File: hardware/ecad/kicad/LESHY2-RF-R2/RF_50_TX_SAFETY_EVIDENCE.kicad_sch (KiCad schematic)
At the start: 98 parts, among them J13 Samtec FTSH-105-01-L-DV-K-P-TR, Q6 Diodes Incorporated 2N7002DW-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, SW5 C&K JS102011SCQN, U101 Diodes Incorporated BAT54-7-F, U102 TLV1821DCKR, U103 TLV1821DCKR, U104 TLV1821DCKR, U105 TCA9535PWR, U106 BAT54ALT1G, U107 BAT54ALT1G, U108 BAT54ALT1G, U109 BAT54ALT1G, U110 BAT54ALT1G, U111 74LVC2G14GV,125, U112 SN74LVC3G07DCUR, U113 SN74LVC08APWR, U114 SN74LVC1G74DCUR, U115 74LVC1G32GV,125, U116 SN74LVC1G17DCKR, U117 Texas Instruments SN74LVC1G06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, U118 SN74LVC1G07DCKR, U119 TPS3808G33DBVR, U120 Texas Instruments TPD4E05U06D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, U121 Texas Instruments MSPM0C1106S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, U122 SN74LVC1G07DCKR, U123 SN74LVC1G07DCKR, U124 Texas Instruments TPS3435CAKA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, U125 SN74LVC1G07DCKR, U126 SN74LVC1G07DCKR, U127 Diodes Incorporated BAT54-7-F, U128 Diodes Incorporated BAT54-7-F

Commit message: Connect RF emergency reset to active RP reset net
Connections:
- net RP_RESET_N renamed RF_RP_RESET_N
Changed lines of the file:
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@@
 		(effects (font (size 1.27 1.27)))
 	)
-	(label "RP_RESET_N"
+	(hierarchical_label "RF_RP_RESET_N"
+		(shape bidirectional)
 		(at 401.32 125.73 0)
 		(effects (font (size 1.27 1.27)))
@@
 		(effects (font (size 1.27 1.27)) (justify right bottom))
 	)
-	(label "RP_RESET_N"
+	(label "RF_RP_RESET_N"
 		(at 990.60 266.70 180)
 		(effects (font (size 1.27 1.27)) (justify right bottom))

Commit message: Review R2 startup and fault-display sequencing
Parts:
- removed R251: Yageo RC0402FR-0710KL, Resistor_SMD:R_0402_1005Metric, symbol Leshy2_R2:yageo_rc0402fr_0710kl
- added R265: Yageo RC0402FR-0710KL, Resistor_SMD:R_0402_1005Metric, symbol Leshy2_R2:yageo_rc0402fr_0710kl
- renumbered R252 to R251, R253 to R252, R254 to R253, R255 to R254, R256 to R255, R257 to R256, R258 to R257, R259 to R258, R260 to R259, R261 to R260, R262 to R261, R263 to R262, R264 to R263, R265 to R264
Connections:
- net EVIDENCE_MASK_UNUSED_P17 is gone; now on net SAFETY_GROUND: U105.20 (P17)
- net FAULT_ASSERT_N: no longer U123.4 (Y)
- net S3_FAULT_RESET_REQUEST: now also R265.1 (END_1)
- net SAFETY_GROUND: now also R265.2 (END_2)
- new net S3_RESET_KILL_GATE: U123.4 (Y)
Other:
- moved on the sheet: R251, R252, R253, R254, R255, R256, R257, R258, R259, R260, R261, R262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

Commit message: Review R2 power transitions and watchdog
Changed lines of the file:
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@@
 		(effects (font (size 1.27 1.27)))
 	)
-	(label "FAULT_KILL"
+	(hierarchical_label "FAULT_KILL"
+		(shape bidirectional)
 		(at 309.88 269.24 0)
 		(effects (font (size 1.27 1.27)))

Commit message: Verify factory-placeable Airband filter
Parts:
- renumbered C254 to C253, C255 to C254, C256 to C255, C257 to C256, C258 to C257, C259 to C258, C260 to C259, C261 to C260, C262 to C261, C263 to C262, C264 to C263, C265 to C264, C266 to C265, C267 to C266, C268 to C267, C269 to C268, C270 to C269, C271 to C270, C272 to C271, C273 to C272, C274 to C273, C275 to C274, C276 to C275, C277 to C276, C278 to C277, C279 to C278, C280 to C279
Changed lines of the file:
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@@
 		(on_board yes)
 		(dnp no)
-		(property "Reference" "C254"
+		(property "Reference" "C253"
 			(at 55.88 44.45 0)
 			(show_name no)
@@
 			(project "LESHY2-RF-R2"
 				(path "/6d47ec69-d4e6-5f0a-87ca-f1fb82f96328"
-					(reference "C254")
+					(reference "C253")
 					(unit 1)
 				)
@@
 		(on_board yes)
 		(dnp no)
-		(property "Reference" "C255"
+		(property "Reference" "C254"
 			(at 147.32 44.45 0)
 			(show_name no)
@@
 			(project "LESHY2-RF-R2"
 				(path "/6d47ec69-d4e6-5f0a-87ca-f1fb82f96328"
-					(reference "C255")
+					(reference "C254")
 					(unit 1)
 				)
@@
 		(on_board yes)
 		(dnp no)
-		(property "Reference" "C256"
+		(property "Reference" "C255"
 			(at 238.76 44.45 0)
 			(show_name no)
@@
 			(project "LESHY2-RF-R2"
 				(path "/6d47ec69-d4e6-5f0a-87ca-f1fb82f96328"
-					(reference "C256")
+					(reference "C255")
 					(unit 1)
 				)
@@
 		(on_board yes)
 		(dnp no)
-		(property "Reference" "C257"
+		(property "Reference" "C256"
 			(at 330.20 44.45 0)
 			(show_name no)
@@
 			(project "LESHY2-RF-R2"
 				(path "/6d47ec69-d4e6-5f0a-87ca-f1fb82f96328"
-					(reference "C257")
+					(reference "C256")
 					(unit 1)
 				)
@@
 		(on_board yes)
 		(dnp no)
-		(property "Reference" "C258"
+		(property "Reference" "C257"
 			(at 421.64 44.45 0)
 			(show_name no)
@@
 			(project "LESHY2-RF-R2"
 				(path "/6d47ec69-d4e6-5f0a-87ca-f1fb82f96328"
-					(reference "C258")
+					(reference "C257")
 					(unit 1)
 				)
@@
 		(on_board yes)
 		(dnp no)
-		(property "Reference" "C259"
+		(property "Reference" "C258"
 			(at 513.08 44.45 0)
 			(show_name no)
@@
 			(project "LESHY2-RF-R2"
 				(path "/6d47ec69-d4e6-5f0a-87ca-f1fb82f96328"
-					(reference "C259")
+					(reference "C258")
 					(unit 1)
 				)
@@
 		(on_board yes)
 		(dnp no)
-		(property "Reference" "C260"
+		(property "Reference" "C259"
 			(at 604.52 44.45 0)
 			(show_name no)
@@
 			(project "LESHY2-RF-R2"
 				(path "/6d47ec69-d4e6-5f0a-87ca-f1fb82f96328"
-					(reference "C260")
+					(reference "C259")
 					(unit 1)
 				)
@@
 		(on_board yes)
 		(dnp no)
-		(property "Reference" "C261"
+		(property "Reference" "C260"
 			(at 695.96 44.45 0)
 			(show_name no)
@@
 			(project "LESHY2-RF-R2"
 				(path "/6d47ec69-d4e6-5f0a-87ca-f1fb82f96328"
-					(reference "C261")
+					(reference "C260")
 					(unit 1)
 				)
@@
 		(on_board yes)
 		(dnp no)
-		(property "Reference" "C262"
+		(property "Reference" "C261"
 			(at 787.40 44.45 0)
 			(show_name no)
@@
 			(project "LESHY2-RF-R2"
 				(path "/6d47ec69-d4e6-5f0a-87ca-f1fb82f96328"
-					(reference "C262")
+					(reference "C261")
 					(unit 1)
 				)
@@
 		(on_board yes)
 		(dnp no)
-		(property "Reference" "C263"
+		(property "Reference" "C262"
 			(at 878.84 44.45 0)
 			(show_name no)
@@
 			(project "LESHY2-RF-R2"
 				(path "/6d47ec69-d4e6-5f0a-87ca-f1fb82f96328"
-					(reference "C263")
+					(reference "C262")
 					(unit 1)
 				)
@@
 		(on_board yes)
 		(dnp no)
-		(property "Reference" "C264"
+		(property "Reference" "C263"
 			(at 970.28 44.45 0)
 			(show_name no)
@@
 			(project "LESHY2-RF-R2"
 				(path "/6d47ec69-d4e6-5f0a-87ca-f1fb82f96328"
-					(reference "C264")
+					(reference "C263")
 					(unit 1)
 				)
@@
 		(on_board yes)
 		(dnp no)
-		(property "Reference" "C265"
+		(property "Reference" "C264"
 			(at 1061.72 44.45 0)
 			(show_name no)
@@
 			(project "LESHY2-RF-R2"
 				(path "/6d47ec69-d4e6-5f0a-87ca-f1fb82f96328"
-					(reference "C265")
+					(reference "C264")
 					(unit 1)
 				)
@@
 		(on_board yes)
 		(dnp no)
-		(property "Reference" "C266"
+		(property "Reference" "C265"
 			(at 55.88 80.01 0)
 			(show_name no)
@@
 			(project "LESHY2-RF-R2"
 				(path "/6d47ec69-d4e6-5f0a-87ca-f1fb82f96328"
-					(reference "C266")
+					(reference "C265")
 					(unit 1)
 				)
@@
 		(on_board yes)
 		(dnp no)
-		(property "Reference" "C267"
+		(property "Reference" "C266"
 			(at 147.32 80.01 0)
 			(show_name no)
@@
 			(project "LESHY2-RF-R2"
 				(path "/6d47ec69-d4e6-5f0a-87ca-f1fb82f96328"
-					(reference "C267")
+					(reference "C266")
 					(unit 1)
 				)
@@
 		(on_board yes)
 		(dnp no)
-		(property "Reference" "C268"
+		(property "Reference" "C267"
 			(at 238.76 80.01 0)
 			(show_name no)
@@
 			(project "LESHY2-RF-R2"
 				(path "/6d47ec69-d4e6-5f0a-87ca-f1fb82f96328"
-					(reference "C268")
+					(reference "C267")
 					(unit 1)
 				)
@@
 		(on_board yes)
 		(dnp no)
-		(property "Reference" "C269"
+		(property "Reference" "C268"
 			(at 330.20 80.01 0)
 			(show_name no)
@@
 			(project "LESHY2-RF-R2"
 				(path "/6d47ec69-d4e6-5f0a-87ca-f1fb82f96328"
-					(reference "C269")
+					(reference "C268")
 					(unit 1)
 				)
@@
 		(on_board yes)
 		(dnp no)
-		(property "Reference" "C270"
+		(property "Reference" "C269"
 			(at 421.64 80.01 0)
 			(show_name no)
@@
 			(project "LESHY2-RF-R2"
 				(path "/6d47ec69-d4e6-5f0a-87ca-f1fb82f96328"
-					(reference "C270")
+					(reference "C269")
 					(unit 1)
 				)
@@
 		(on_board yes)
 		(dnp no)
-		(property "Reference" "C271"
+		(property "Reference" "C270"
 			(at 513.08 80.01 0)
 			(show_name no)
@@
 			(project "LESHY2-RF-R2"
 				(path "/6d47ec69-d4e6-5f0a-87ca-f1fb82f96328"
-					(reference "C271")
+					(reference "C270")
 					(unit 1)
 				)
@@
 		(on_board yes)
 		(dnp no)
-		(property "Reference" "C272"
+		(property "Reference" "C271"
 			(at 604.52 80.01 0)
 			(show_name no)
@@
 			(project "LESHY2-RF-R2"
 				(path "/6d47ec69-d4e6-5f0a-87ca-f1fb82f96328"
-					(reference "C272")
+					(reference "C271")
 					(unit 1)
 				)
@@
 		(on_board yes)
 		(dnp no)
-		(property "Reference" "C273"
+		(property "Reference" "C272"
 			(at 695.96 80.01 0)
 			(show_name no)
@@
 			(project "LESHY2-RF-R2"
 				(path "/6d47ec69-d4e6-5f0a-87ca-f1fb82f96328"
-					(reference "C273")
+					(reference "C272")
 					(unit 1)
 				)
@@
 		(on_board yes)
 		(dnp no)
-		(property "Reference" "C274"
+		(property "Reference" "C273"
 			(at 787.40 80.01 0)
 			(show_name no)
@@
 			(project "LESHY2-RF-R2"
 				(path "/6d47ec69-d4e6-5f0a-87ca-f1fb82f96328"
-					(reference "C274")
+					(reference "C273")
 					(unit 1)
 				)
@@
 		(on_board yes)
 		(dnp no)
-		(property "Reference" "C275"
+		(property "Reference" "C274"
 			(at 878.84 80.01 0)
 			(show_name no)
@@
 			(project "LESHY2-RF-R2"
 				(path "/6d47ec69-d4e6-5f0a-87ca-f1fb82f96328"
-					(reference "C275")
+					(reference "C274")
 					(unit 1)
 				)
@@
 		(on_board yes)
 		(dnp no)
-		(property "Reference" "C276"
+		(property "Reference" "C275"
 			(at 970.28 80.01 0)
 			(show_name no)
@@
 			(project "LESHY2-RF-R2"
 				(path "/6d47ec69-d4e6-5f0a-87ca-f1fb82f96328"
-					(reference "C276")
+					(reference "C275")
 					(unit 1)
 				)
@@
 		(on_board yes)
 		(dnp no)
-		(property "Reference" "C277"
+		(property "Reference" "C276"
 			(at 1061.72 80.01 0)
 			(show_name no)
@@
 			(project "LESHY2-RF-R2"
 				(path "/6d47ec69-d4e6-5f0a-87ca-f1fb82f96328"
-					(reference "C277")
+					(reference "C276")
 					(unit 1)
 				)
@@
 		(on_board yes)
 		(dnp no)
-		(property "Reference" "C278"
+		(property "Reference" "C277"
 			(at 55.88 115.57 0)
 			(show_name no)
@@
 			(project "LESHY2-RF-R2"
 				(path "/6d47ec69-d4e6-5f0a-87ca-f1fb82f96328"
-					(reference "C278")
+					(reference "C277")
 					(unit 1)
 				)
@@
 		(on_board yes)
 		(dnp no)
-		(property "Reference" "C279"
+		(property "Reference" "C278"
 			(at 147.32 115.57 0)
 			(show_name no)
@@
 			(project "LESHY2-RF-R2"
 				(path "/6d47ec69-d4e6-5f0a-87ca-f1fb82f96328"
-					(reference "C279")
+					(reference "C278")
 					(unit 1)
 				)
@@
 		(on_board yes)
 		(dnp no)
-		(property "Reference" "C280"
+		(property "Reference" "C279"
 			(at 238.76 115.57 0)
 			(show_name no)
@@
 			(project "LESHY2-RF-R2"
 				(path "/6d47ec69-d4e6-5f0a-87ca-f1fb82f96328"
-					(reference "C280")
-					(unit 1)
-				)
+					(reference "C279")
+					(unit 1)
+				)

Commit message: Complete current R2 schematic and sourcing revalidation
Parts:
- renumbered C253 to C262, C254 to C263, C255 to C264, C256 to C265, C257 to C266, C258 to C267, C259 to C268, C260 to C269, C261 to C270, C262 to C271, C263 to C272, C264 to C273, C265 to C274, C266 to C275, C267 to C276, C268 to C277, C269 to C278, C270 to C279, C271 to C280, C272 to C281, C273 to C282, C274 to C283, C275 to C284, C276 to C285, C277 to C286, C278 to C287, C279 to C288, R240 to R249, R241 to R250, R242 to R251, R243 to R252, R244 to R253, R245 to R254, R246 to R255, R247 to R256, R248 to R257, R249 to R258, R250 to R259, R251 to R260, R252 to R261, R253 to R262, R254 to R263, R255 to R264, R256 to R265, R257 to R266, R258 to R267, R259 to R268, R260 to R269, R261 to R270, R262 to R271, R263 to R272, R264 to R273, R265 to R274, R266 to R275, R267 to R276, R268 to R277, R269 to R278, R270 to R279, R271 to R280, R272 to R281, R273 to R282, R274 to R283, R275 to R284, R276 to R285, R277 to R286, R278 to R287, R279 to R288, U101 to U107, U102 to U108, U103 to U109, U104 to U110, U105 to U111, U106 to U112, U107 to U113, U108 to U114, U109 to U115, U110 to U116, U111 to U117, U112 to U118, U113 to U119, U114 to U120, U115 to U121, U116 to U122, U117 to U123, U118 to U124, U119 to U125, U120 to U126, U121 to U127, U122 to U128, U123 to U129, U124 to U130, U125 to U131, U126 to U132, U127 to U133, U128 to U134
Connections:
- net SAFETY_GROUND: no longer U111.20 (P17)
- net EV_N9_U219_NFC: now reaches U116.2 (K2)
- net EV_N9_U219_NFC: now also U111.20 (P17)
- no-connect marks 22 -> 21

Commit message: Canonicalize physical ground anchors
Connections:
- net SAFETY_ESD_GROUND is gone; now on net POWER_GROUND: U126.3 (GND_3), U126.8 (GND_8)
- net SAFETY_GROUND is gone; now on net POWER_GROUND: C262.2 (END_2), C263.2 (END_2), C264.2 (END_2), C265.2 (END_2), C266.2 (END_2), C268.2 (END_2), C269.2 (END_2), C270.2 (END_2), C271.2 (END_2), C272.2 (END_2), C273.2 (END_2), C274.2 (END_2), C275.2 (END_2), C276.2 (END_2), C277.2 (END_2), C278.2 (END_2), C279.2 (END_2), C280.2 (END_2), C281.2 (END_2), C282.2 (END_2), C283.2 (END_2), C284.2 (END_2), C285.2 (END_2), C286.2 (END_2), C287.2 (END_2), C288.2 (END_2), J13.1 (P1), J13.7 (P7), J13.9 (P9), Q6.1 (S2), Q6.2 (G2), Q6.4 (S1), R250.2 (END_2), R253.2 (END_2), R255.2 (END_2), R256.2 (END_2), R257.2 (END_2), R258.2 (END_2), R262.2 (END_2), R273.2 (END_2), R274.2 (END_2), R276.2 (END_2), R280.2 (END_2), R283.2 (END_2), R285.2 (END_2), R287.2 (END_2), U108.2 (VMINUS), U109.2 (VMINUS), U110.2 (VMINUS), U111.12 (GND), U111.2 (A1), U111.21 (A0), U111.3 (A2), U117.2 (GND), U118.4 (GND), U119.7 (GND), U120.4 (GND), U121.3 (GND), U122.3 (GND), U123.3 (GND), U124.3 (GND), U125.2 (GND), U127.7 (VSS), U128.3 (GND), U129.3 (GND), U130.1 (SET0), U130.4 (GND), U130.5 (SET1), U131.3 (GND), U132.3 (GND)

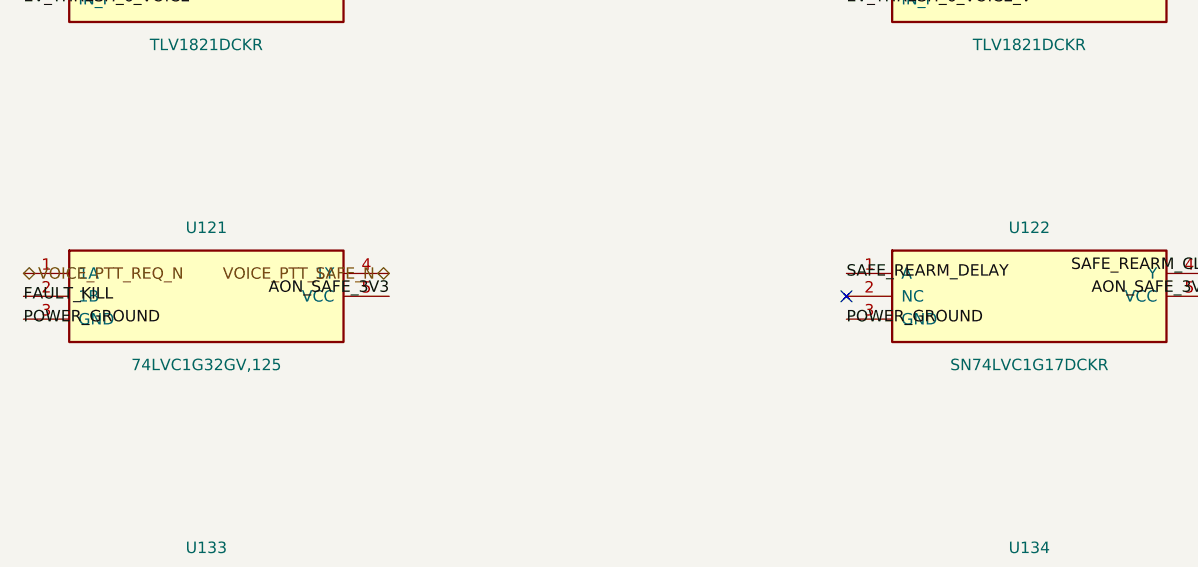
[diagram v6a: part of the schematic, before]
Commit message: Fix exact pin maps and RP flash power; add typed electrical review
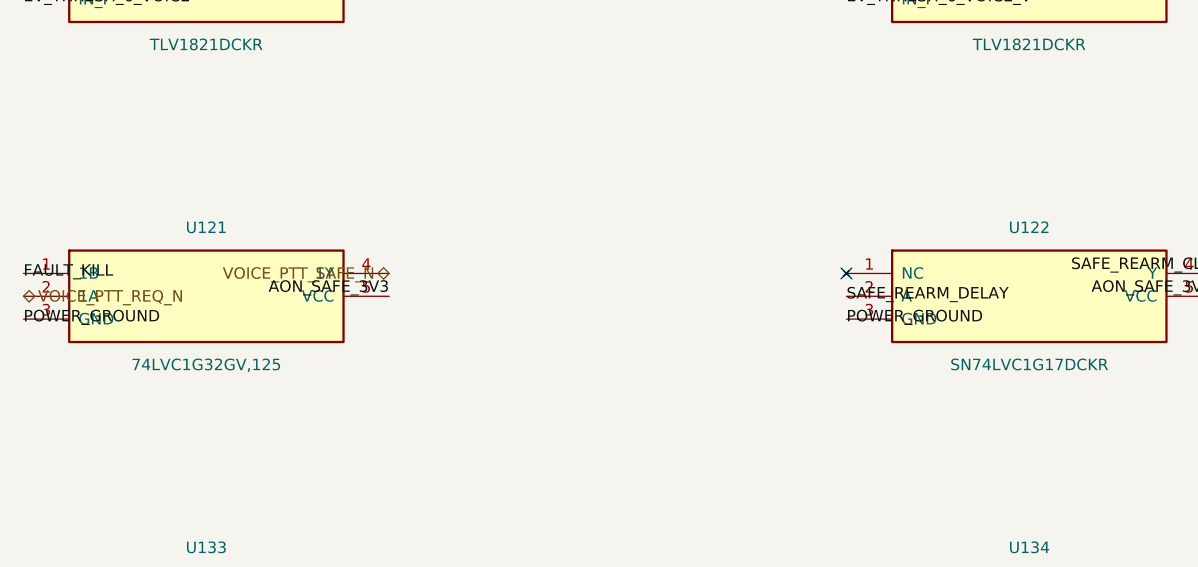
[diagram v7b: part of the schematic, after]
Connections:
- net FAULT_KILL: now also U121.1 (1B); no longer U121.2 (1B)
- net SAFE_REARM_DELAY: now also U122.2 (A); no longer U122.1 (A)
- net VOICE_PTT_REQ_N: now also U121.2 (1A); no longer U121.1 (1A)
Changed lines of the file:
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@@
 		)
+	)
+	(label "FAULT_KILL"
+		(at 35.56 298.45 0)
+		(effects (font (size 1.27 1.27)))
 	)
 	(hierarchical_label "VOICE_PTT_REQ_N"
 		(shape bidirectional)
-		(at 35.56 298.45 0)
-		(effects (font (size 1.27 1.27)))
-	)
-	(label "FAULT_KILL"
 		(at 35.56 300.99 0)
 		(effects (font (size 1.27 1.27)))
@@
 		)
 	)
+	(no_connect (at 127.00 298.45)
+	)
 	(label "SAFE_REARM_DELAY"
-		(at 127.00 298.45 0)
+		(at 127.00 300.99 0)
 		(effects (font (size 1.27 1.27)))
 	)
-	(no_connect (at 127.00 300.99)
-	)
 	(label "POWER_GROUND"

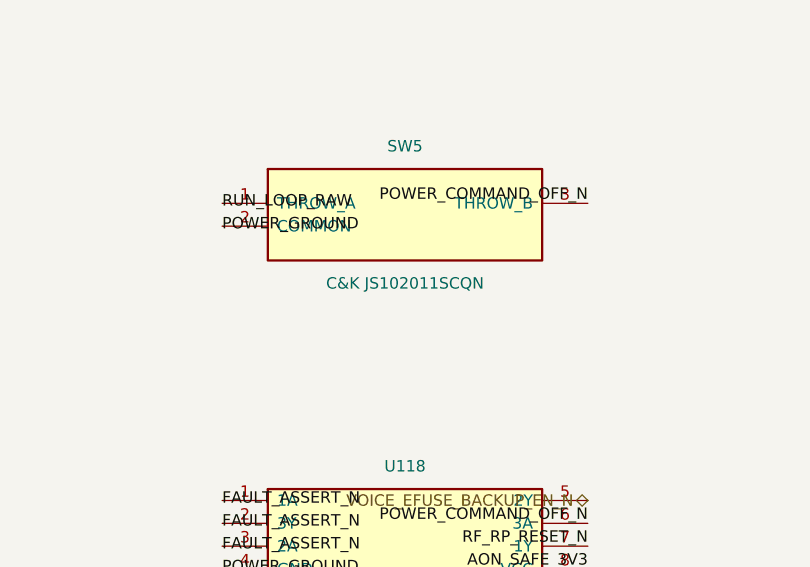
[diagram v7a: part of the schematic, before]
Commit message: Integrate reviewed R2 interface geometry and refresh guarded PCB evidence
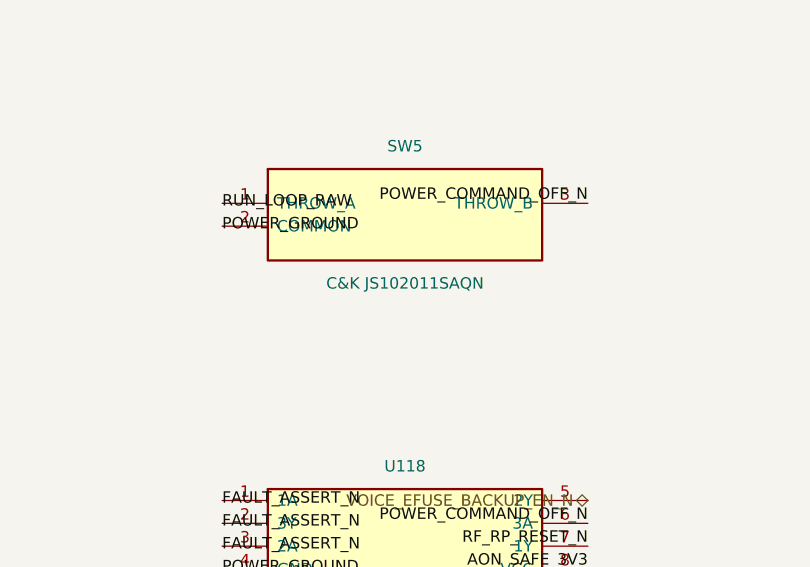
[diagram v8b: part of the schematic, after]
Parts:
- SW5: value C&K JS102011SCQN -> C&K JS102011SAQN; footprint Leshy2:JS102011SCQN -> Button_Switch_SMD:SW_SPDT_CK_JS102011SAQN; symbol Leshy2_R2:ck_js102011scqn -> Leshy2_R2:ck_js102011saqn
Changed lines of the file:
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@@
 	)
 	(symbol
-		(lib_id "Leshy2_R2:ck_js102011scqn")
+		(lib_id "Leshy2_R2:ck_js102011saqn")
 		(at 970.28 229.87 0)
 		(unit 1)
@@
 			(effects (font (size 1.27 1.27)))
 		)
-		(property "Value" "C&K JS102011SCQN"
+		(property "Value" "C&K JS102011SAQN"
 			(at 970.28 237.49 0)
 			(show_name no)
@@
 			(effects (font (size 1.27 1.27)))
 		)
-		(property "Footprint" "Leshy2:JS102011SCQN"
+		(property "Footprint" "Button_Switch_SMD:SW_SPDT_CK_JS102011SAQN"
 			(at 970.28 229.87 0)
 			(show_name no)
@@
 			(effects (font (size 1.27 1.27)))
 		)
-		(property "Description" "ck_js102011scqn"
+		(property "Description" "ck_js102011saqn"
 			(at 970.28 229.87 0)
 			(show_name no)
